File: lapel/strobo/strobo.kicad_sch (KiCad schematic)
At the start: 31 parts, among them J1 USB_C_Receptacle_PowerOnly_6P, U1 ICM7556, U2 MCP73831-2-MC

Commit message: meh
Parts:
- D1, D2, D3, D4, D5, D6, D7: footprint (none) -> LED_SMD:LED_0805_2012Metric_Pad1.15x1.40mm_HandSolder
- U1: footprint (none) -> Package_SO:SOIC-14_3.9x8.7mm_P1.27mm
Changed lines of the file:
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@@
 			)
 		)
-		(property "Footprint" ""
+		(property "Footprint" "LED_SMD:LED_0805_2012Metric_Pad1.15x1.40mm_HandSolder"
 			(at 95.25 92.71 0)
 			(hide yes)
@@
 			)
 		)
-		(property "Footprint" ""
+		(property "Footprint" "LED_SMD:LED_0805_2012Metric_Pad1.15x1.40mm_HandSolder"
 			(at 106.68 34.29 0)
 			(hide yes)
@@
 			)
 		)
-		(property "Footprint" ""
+		(property "Footprint" "Package_SO:SOIC-14_3.9x8.7mm_P1.27mm"
 			(at 48.26 76.2 0)
 			(hide yes)
@@
 			)
 		)
-		(property "Footprint" ""
+		(property "Footprint" "LED_SMD:LED_0805_2012Metric_Pad1.15x1.40mm_HandSolder"
 			(at 77.47 100.33 0)
 			(hide yes)
@@
 			)
 		)
-		(property "Footprint" ""
+		(property "Footprint" "LED_SMD:LED_0805_2012Metric_Pad1.15x1.40mm_HandSolder"
 			(at 115.57 92.71 0)
 			(hide yes)
@@
 			)
 		)
-		(property "Footprint" ""
+		(property "Footprint" "LED_SMD:LED_0805_2012Metric_Pad1.15x1.40mm_HandSolder"
 			(at 67.31 100.33 0)
 			(hide yes)
@@
 			)
 		)
-		(property "Footprint" ""
+		(property "Footprint" "LED_SMD:LED_0805_2012Metric_Pad1.15x1.40mm_HandSolder"
 			(at 87.63 100.33 0)
 			(hide yes)
@@
 			)
 		)
-		(property "Footprint" ""
+		(property "Footprint" "LED_SMD:LED_0805_2012Metric_Pad1.15x1.40mm_HandSolder"
 			(at 105.41 92.71 0)
 			(hide yes)
@@
 			)
 		)
-		(property "Footprint" ""
+		(property "Footprint" "Package_SO:SOIC-14_3.9x8.7mm_P1.27mm"
 			(at 48.26 116.84 0)
 			(hide yes)

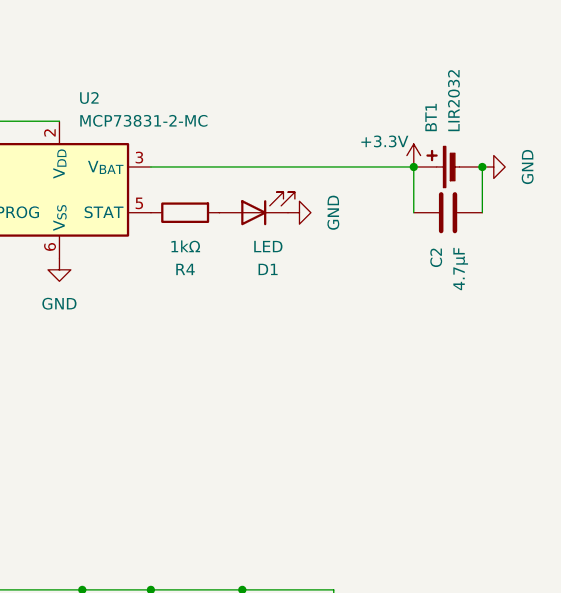
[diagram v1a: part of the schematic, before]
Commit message: feat(strobo): PCB layout, schematic updates, and fabrication outputs
- Add SW_SPDT symbol to schematic
- Major PCB layout rework (routing, component placement)
- Add DRC exclusions with justification notes
- Configure ngspice simulation workbook
- Set plot output path to dist/
- Change dimension units to mm
- Add ICM7556 custom component library
- Add freerouting session file and round-tracks config
- Add fabrication outputs: gerbers, drill files, BOM, iBOM, zip
- Add kit.yml project config
- Add .pi/gsd agent config and workflows
- Update .gitignore: ignore lock files, .history/, temp-freerouting.dsn
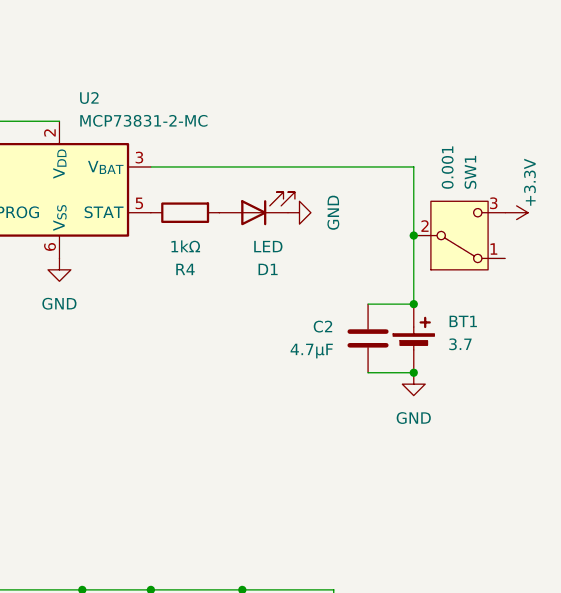
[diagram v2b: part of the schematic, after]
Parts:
- added SW1: 0.001, Button_Switch_THT:SW_Slide_SPDT_Angled_CK_OS102011MA1Q, symbol Switch:SW_SPDT
- BT1: value LIR2032 -> 3.7
- J1: footprint Connector_USB:USB_C_Receptacle_G-Switch_GT-USB-7025 -> Connector_USB:USB_C_Receptacle_GCT_USB4125-xx-x-0190_6P_TopMnt_Horizontal
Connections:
- net +3.3V: now also SW1.3 (C); no longer BT1.1 (+), C2.1, U2.3 (V_{BAT}), U2.4 (V_{BAT})
- new net: BT1.1 (+), C2.1, SW1.2 (B), U2.3 (V_{BAT}), U2.4 (V_{BAT})
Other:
- moved on the sheet: BT1, C2
